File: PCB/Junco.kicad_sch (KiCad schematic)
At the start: 202 parts, among them J1 AudioJack4, J2 AudioJack4, SW1 SW_Push, SW10 SW_Push, SW11 SW_Push, SW12 SW_Push, SW13 SW_Push, SW14 SW_Push, SW15 SW_Push, SW16 SW_Push, SW17 SW_Push, SW18 SW_Push, SW19 SW_MX_Hotswap_Rotary, SW2 SW_Push, SW20 SW_Push, SW21 SW_Push, SW22 SW_Push, SW23 SW_Push, SW24 SW_Push, SW25 SW_Push, SW26 SW_Push, SW27 SW_Push, SW28 SW_Push, SW29 SW_Push, SW3 SW_Push, SW30 RotaryEncoder_Switch, SW31 SW_Push, SW32 SW_Push, SW33 SW_Push, SW34 SW_Push, SW35 SW_Push, SW36 SW_Push, SW37 SW_Push, SW38 SW_Push, SW39 SW_Push, SW4 SW_Push, SW40 SW_Push, SW41 SW_Push, SW42 SW_Push, SW43 SW_Push, SW44 SW_Push, SW45 SW_Push, SW46 SW_Push, SW47 SW_Push, SW48 SW_Push, SW49 SW_MX_Hotswap_Rotary, SW5 SW_Push, SW50 SW_Push, SW51 SW_Push, SW52 SW_Push, SW53 SW_Push, SW54 SW_Push, SW55 SW_Push, SW56 SW_Push, SW57 SW_Push, SW58 SW_Push, SW59 SW_Push, SW6 SW_Push, SW60 RotaryEncoder_Switch, SW7 SW_Push, SW8 SW_Push, SW9 SW_Push, U1 Pico, U2 SN74AHCT1G125, U3 Pico, U4 SN74AHCT1G125

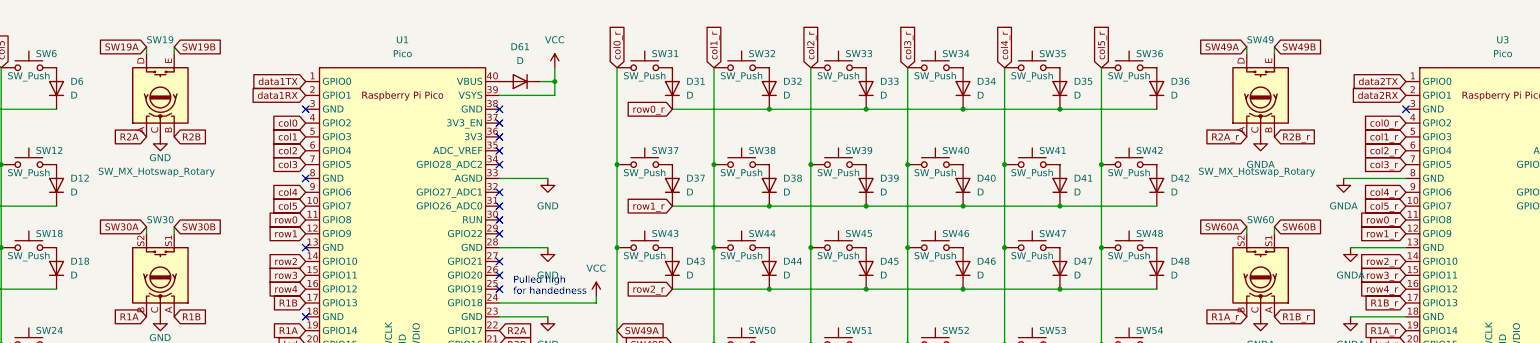
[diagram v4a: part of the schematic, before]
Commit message: Updated corner encoders Created flipped encoder/switch combo footprint Created short offset LED for encoder/switch combo Encoder routing Added build notes
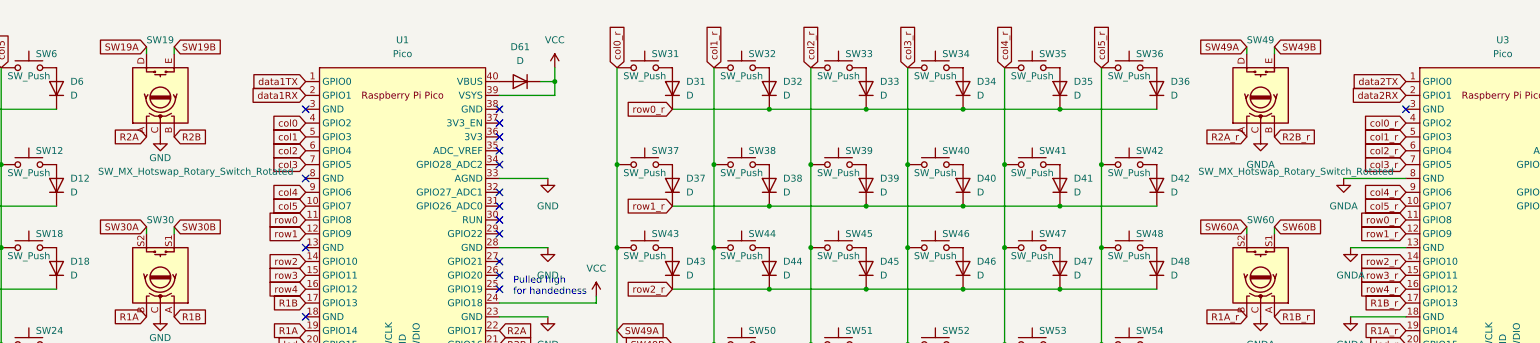
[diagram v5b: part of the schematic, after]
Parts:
- SK68XX_Mini27: value SK68XXMini -> SK68XXMini_Short_Offset_for_Rotary_Encoder; footprint Junco:SK68XXMini_Offset -> Junco:SK68XXMini_Short_Offset_for_Rotary_Encoder
- SK68XX_Mini64: footprint Junco:SK68XXMini_Offset -> Junco:SK68XXMini_Short_Offset_for_Rotary_Encoder
- SW19, SW49: value SW_MX_Hotswap_Rotary -> SW_MX_Hotswap_Rotary_Switch_Rotated; footprint Junco:SW_MX_Hotswap_Rotary -> Junco:SW_MX_Hotswap_Rotary_Switch_Rotated
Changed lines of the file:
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@@
       (effects (font (size 1.27 1.27)) (justify left))
     )
-    (property "Value" "SW_MX_Hotswap_Rotary" (at 322.58 40.64 0)
-      (effects (font (size 1.27 1.27)) (justify left))
-    )
-    (property "Footprint" "Junco:SW_MX_Hotswap_Rotary" (at 316.23 36.83 0)
+    (property "Value" "SW_MX_Hotswap_Rotary_Switch_Rotated" (at 322.58 40.64 0)
+      (effects (font (size 1.27 1.27)) (justify left))
+    )
+    (property "Footprint" "Junco:SW_MX_Hotswap_Rotary_Switch_Rotated" (at 316.23 36.83 0)
       (effects (font (size 1.27 1.27)) hide)
     )
@@
       (effects (font (size 1.27 1.27)) hide)
     )
-    (property "Footprint" "Junco:SK68XXMini_Offset" (at 303.53 205.74 0)
+    (property "Footprint" "Junco:SK68XXMini_Short_Offset_for_Rotary_Encoder" (at 303.53 205.74 0)
       (effects (font (size 1.27 1.27)) hide)
     )
@@
       (effects (font (size 1.27 1.27)))
     )
-    (property "Value" "SK68XXMini" (at 83.82 221.996 0)
-      (effects (font (size 1.27 1.27)) hide)
-    )
-    (property "Footprint" "Junco:SK68XXMini_Offset" (at 80.01 215.9 0)
+    (property "Value" "SK68XXMini_Short_Offset_for_Rotary_Encoder" (at 83.82 221.996 0)
+      (effects (font (size 1.27 1.27)) hide)
+    )
+    (property "Footprint" "Junco:SK68XXMini_Short_Offset_for_Rotary_Encoder" (at 80.01 215.9 0)
       (effects (font (size 1.27 1.27)) hide)
     )
@@
       (effects (font (size 1.27 1.27)) (justify left))
     )
-    (property "Value" "SW_MX_Hotswap_Rotary" (at 120.65 40.64 0)
-      (effects (font (size 1.27 1.27)) (justify left))
-    )
-    (property "Footprint" "Junco:SW_MX_Hotswap_Rotary" (at 114.3 36.83 0)
-      (effects (font (size 1.27 1.27)) hide)
-    )
+    (property "Value" "SW_MX_Hotswap_Rotary_Switch_Rotated" (at 120.65 40.64 0)
+      (effects (font (size 1.27 1.27)) (justify left))
+    )
+    (property "Footprint" "Junco:SW_MX_Hotswap_Rotary_Switch_Rotated" (at 114.3 36.83 0)
+      (effects (font (size 1.27 1.27)) hide)
+    )

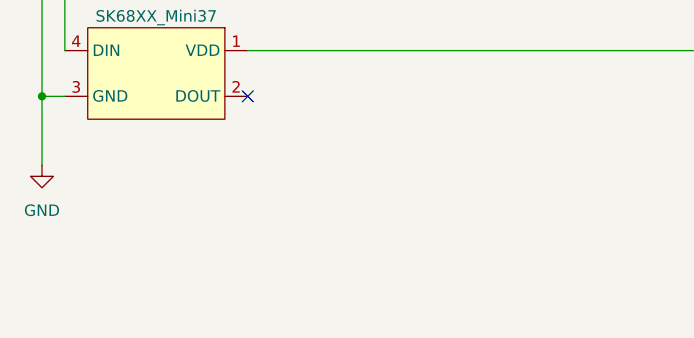
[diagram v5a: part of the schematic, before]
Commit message: Added fiducials
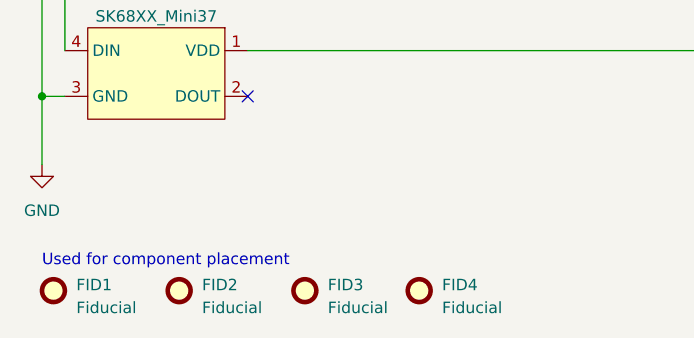
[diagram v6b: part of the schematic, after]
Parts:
- added FID1, FID2, FID3, FID4: Fiducial, Fiducial:Fiducial_1mm_Mask2mm, symbol Mechanical:Fiducial
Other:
- note added: "Used for component placement"
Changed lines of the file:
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@@
     (stroke (width 0) (type default))
   )
+  (text "Used for component placement" (at 15.24 278.13 0)
+    (effects (font (size 1.27 1.27)) (justify left bottom))
+  )
   (text "JUNCO KEYBOARD\n" (at 322.58 266.7 0)
     (effects (font (size 5 5) (thickness 2) bold) (justify left bottom))
@@
     )
   )
+  (symbol (lib_id "Mechanical:Fiducial") (at 44.45 280.67 0) (unit 1)
+    (in_bom yes) (on_board yes) (dnp no) (fields_autoplaced)
+    (property "Reference" "FID3" (at 46.99 280.035 0)
+      (effects (font (size 1.27 1.27)) (justify left))
+    )
+    (property "Value" "Fiducial" (at 46.99 282.575 0)
+      (effects (font (size 1.27 1.27)) (justify left))
+    )
+    (property "Footprint" "Fiducial:Fiducial_1mm_Mask2mm" (at 44.45 280.67 0)
+      (effects (font (size 1.27 1.27)) hide)
+    )
+    (property "Datasheet" "~" (at 44.45 280.67 0)
+      (effects (font (size 1.27 1.27)) hide)
+    )
+    (instances
+      (project "Junco"
+        (path "/c55ab6a7-e623-4136-bc89-8abb0d1fdb80"
+          (reference "FID3") (unit 1)
+        )
+      )
+    )
+  )
   (symbol (lib_id "Switch:SW_Push") (at 292.1 21.59 0) (unit 1)
     (in_bom yes) (on_board yes) (dnp no) (fields_autoplaced)
@@
     )
   )
+  (symbol (lib_id "Mechanical:Fiducial") (at 16.51 280.67 0) (unit 1)
+    (in_bom yes) (on_board yes) (dnp no) (fields_autoplaced)
+    (property "Reference" "FID1" (at 19.05 280.035 0)
+      (effects (font (size 1.27 1.27)) (justify left))
+    )
+    (property "Value" "Fiducial" (at 19.05 282.575 0)
+      (effects (font (size 1.27 1.27)) (justify left))
+    )
+    (property "Footprint" "Fiducial:Fiducial_1mm_Mask2mm" (at 16.51 280.67 0)
+      (effects (font (size 1.27 1.27)) hide)
+    )
+    (property "Datasheet" "~" (at 16.51 280.67 0)
+      (effects (font (size 1.27 1.27)) hide)
+    )
+    (instances
+      (project "Junco"
+        (path "/c55ab6a7-e623-4136-bc89-8abb0d1fdb80"
+          (reference "FID1") (unit 1)
+        )
+      )
+    )
+  )
   (symbol (lib_id "power:GNDA") (at 334.01 67.31 0) (unit 1)
     (in_bom yes) (on_board yes) (dnp no) (fields_autoplaced)
@@
     )
   )
+  (symbol (lib_id "Mechanical:Fiducial") (at 30.48 280.67 0) (unit 1)
+    (in_bom yes) (on_board yes) (dnp no) (fields_autoplaced)
+    (property "Reference" "FID2" (at 33.02 280.035 0)
+      (effects (font (size 1.27 1.27)) (justify left))
+    )
+    (property "Value" "Fiducial" (at 33.02 282.575 0)
+      (effects (font (size 1.27 1.27)) (justify left))
+    )
+    (property "Footprint" "Fiducial:Fiducial_1mm_Mask2mm" (at 30.48 280.67 0)
+      (effects (font (size 1.27 1.27)) hide)
+    )
+    (property "Datasheet" "~" (at 30.48 280.67 0)
+      (effects (font (size 1.27 1.27)) hide)
+    )
+    (instances
+      (project "Junco"
+        (path "/c55ab6a7-e623-4136-bc89-8abb0d1fdb80"
+          (reference "FID2") (unit 1)
+        )
+      )
+    )
+  )
   (symbol (lib_id "Junco:SK68XXMini") (at 55.88 236.22 0) (unit 1)
     (in_bom yes) (on_board yes) (dnp no) (fields_autoplaced)
@@
         )
       )
+    )
+  )
+  (symbol (lib_id "Mechanical:Fiducial") (at 57.15 280.67 0) (unit 1)
+    (in_bom yes) (on_board yes) (dnp no) (fields_autoplaced)
+    (property "Reference" "FID4" (at 59.69 280.035 0)
+      (effects (font (size 1.27 1.27)) (justify left))
+    )
+    (property "Value" "Fiducial" (at 59.69 282.575 0)
+      (effects (font (size 1.27 1.27)) (justify left))
+    )
+    (property "Footprint" "Fiducial:Fiducial_1mm_Mask2mm" (at 57.15 280.67 0)
+      (effects (font (size 1.27 1.27)) hide)
+    )
+    (property "Datasheet" "~" (at 57.15 280.67 0)
+      (effects (font (size 1.27 1.27)) hide)
+    )
+    (instances
+      (project "Junco"
+        (path "/c55ab6a7-e623-4136-bc89-8abb0d1fdb80"
+          (reference "FID4") (unit 1)
+        )
+      )
